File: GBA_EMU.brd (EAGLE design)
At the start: 130.7 x 72.9 mm, 82 parts, among them J1 USB-MINIB-5PIN, J2 AVR_SPI, SW1 LEFT, SW2 RIGHT, SW3 PWR_SWITCH, U1 MIC7221, U2 MICROCHIP_MCP1642B-ADJ, U4 LM4875, U5 Mic5365-2.8Y, U7 AZV321, X2 HEADPHONE

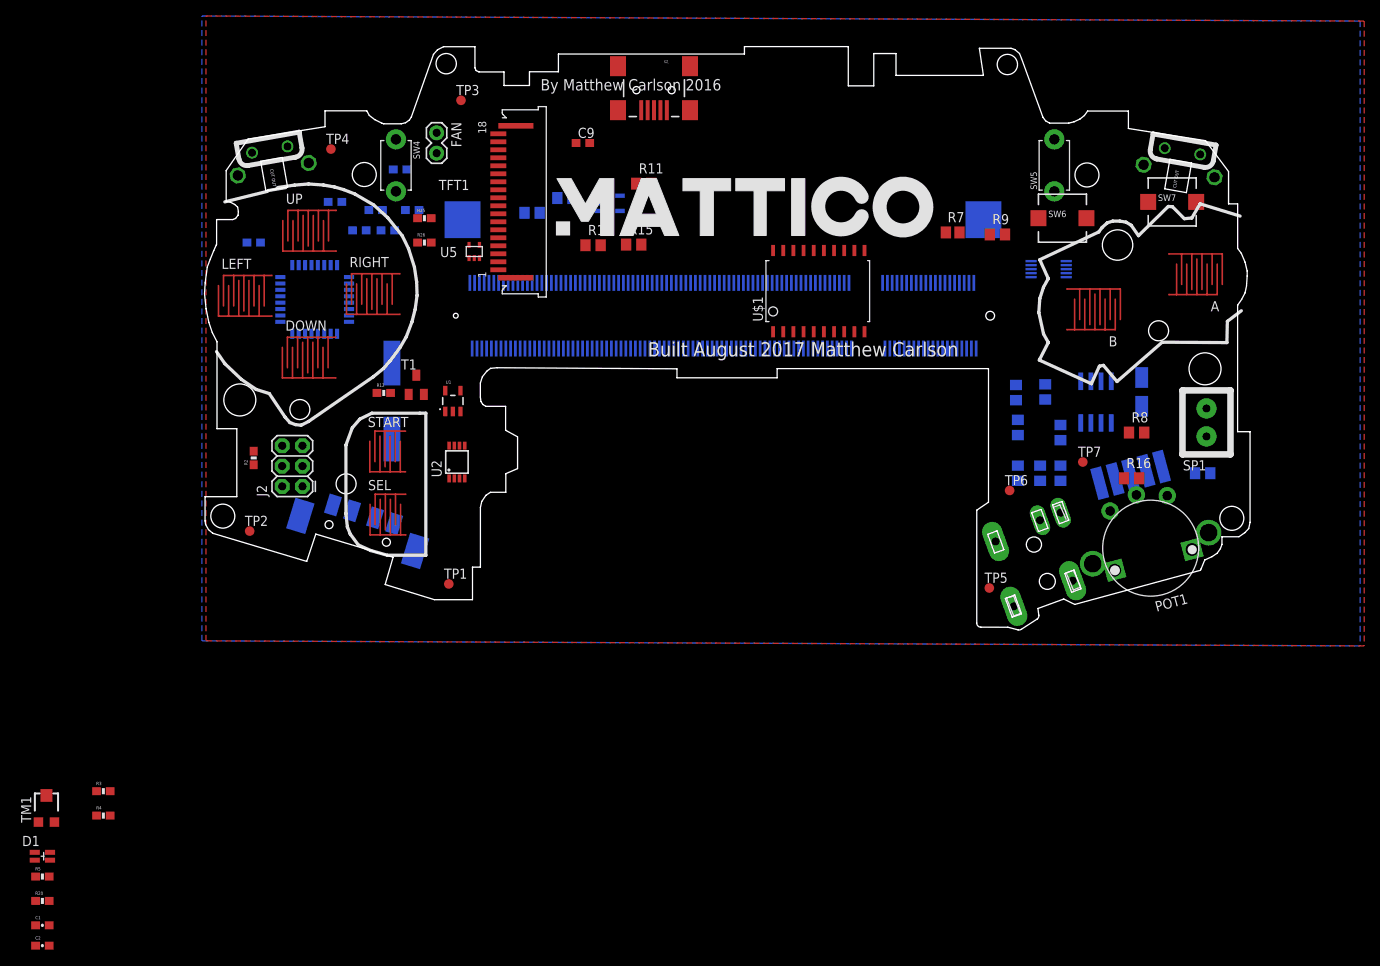
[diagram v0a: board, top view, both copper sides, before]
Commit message: added new parts and routed bus switch
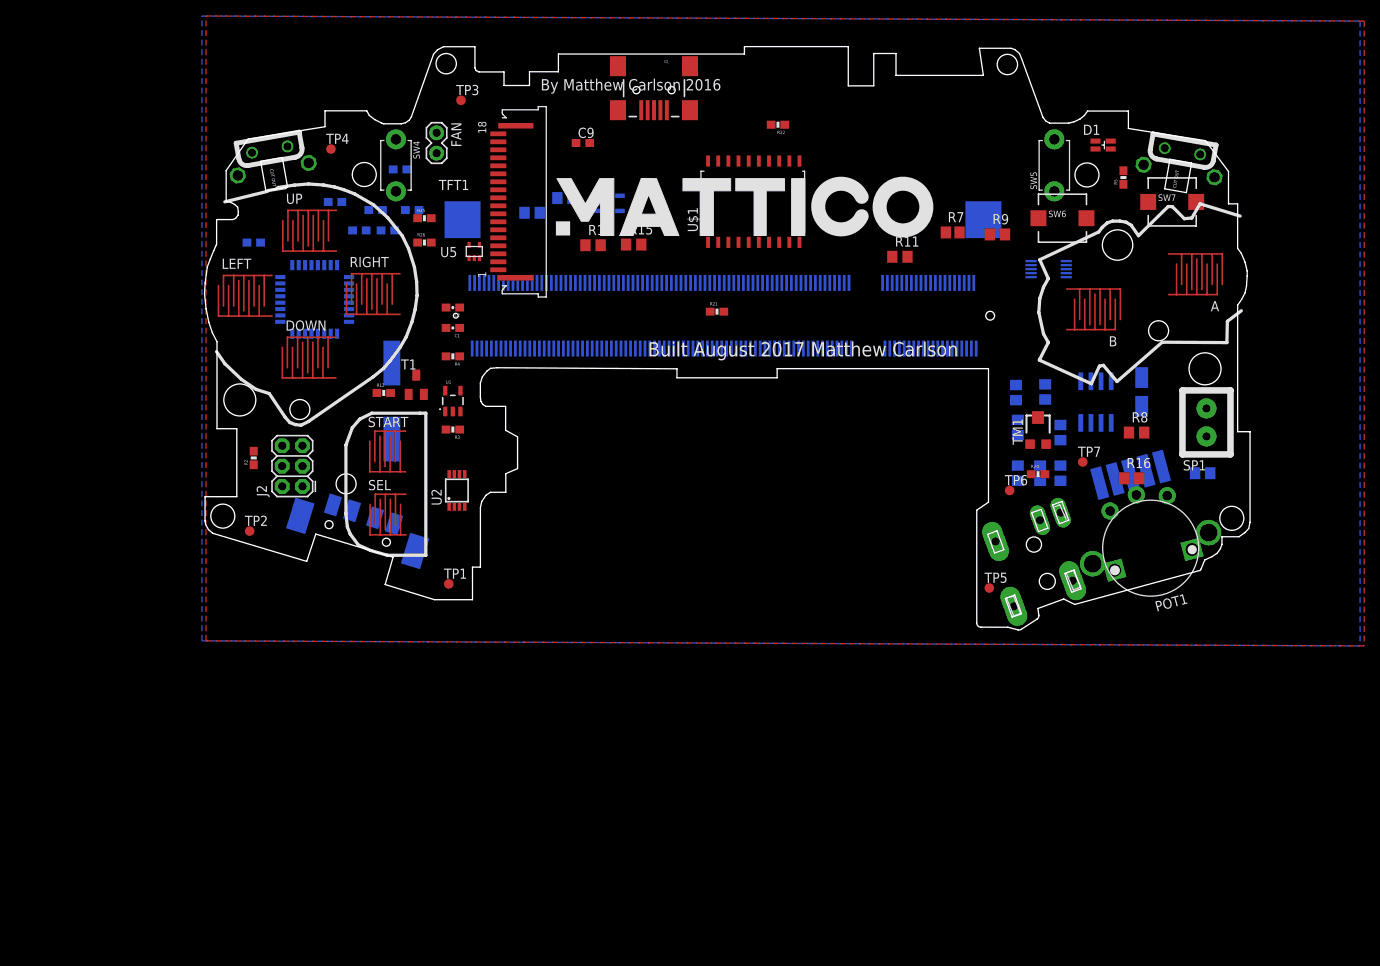
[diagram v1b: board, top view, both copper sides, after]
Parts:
- added R21, R22: 4.7K, SparkFun-Resistors:0603-RES
- moved R5 160.9 mm to (136.1, 65.5), turned to 90 degrees
- moved D1 159.6 mm to (133.6, 69.6)
- moved R20 135.4 mm to (125.5, 28.4)
- moved TM1 132.7 mm to (125.5, 34.0)
- moved C2 94.8 mm to (52.3, 49.3), turned to 180 degrees
- moved C1 90.6 mm to (52.3, 46.7), turned to 180 degrees
- moved R4 72.1 mm to (52.3, 43.2), turned to 180 degrees
- moved R3 62.9 mm to (52.3, 34.0), turned to 180 degrees
- moved R11 33.3 mm to (108.2, 55.6)
- moved U$1 13.8 mm to (84.2, 62.5)
- moved U2 3.56 mm to (52.8, 26.4)
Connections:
- removed net MOSI: TFT1.6
- removed net SCLK: TFT1.3
- removed net VCC: U$1.P$20
- removed net Z_BTN: COPRO.14
- new net COPRO_DC: COPRO.20, U$1.P$8
- new net COPRO_TFT_RESET: COPRO.14, U$1.P$6
- new net N$10: R22.1, U$1.P$19
- new net N$18: R21.1, U$1.P$1
- new net PI_DC: U$1.P$17
- new net PI_MOSI: U$1.P$13
- new net PI_SCK: U$1.P$11
- new net PI_TFT_RESET: U$1.P$15
- new net TFT_MOSI: TFT1.6, U$1.P$16, U$1.P$7
- new net TFT_SCLK: TFT1.3, U$1.P$18, U$1.P$9
- net 3.3V: now also R21.2, R22.2, U$1.P$20
- net COPRO_MOSI: now also U$1.P$4
- net COPRO_SCK: now also U$1.P$2
- net TFT_DC: now also U$1.P$12, U$1.P$3
- net TFT_RESET: now also U$1.P$14, U$1.P$5

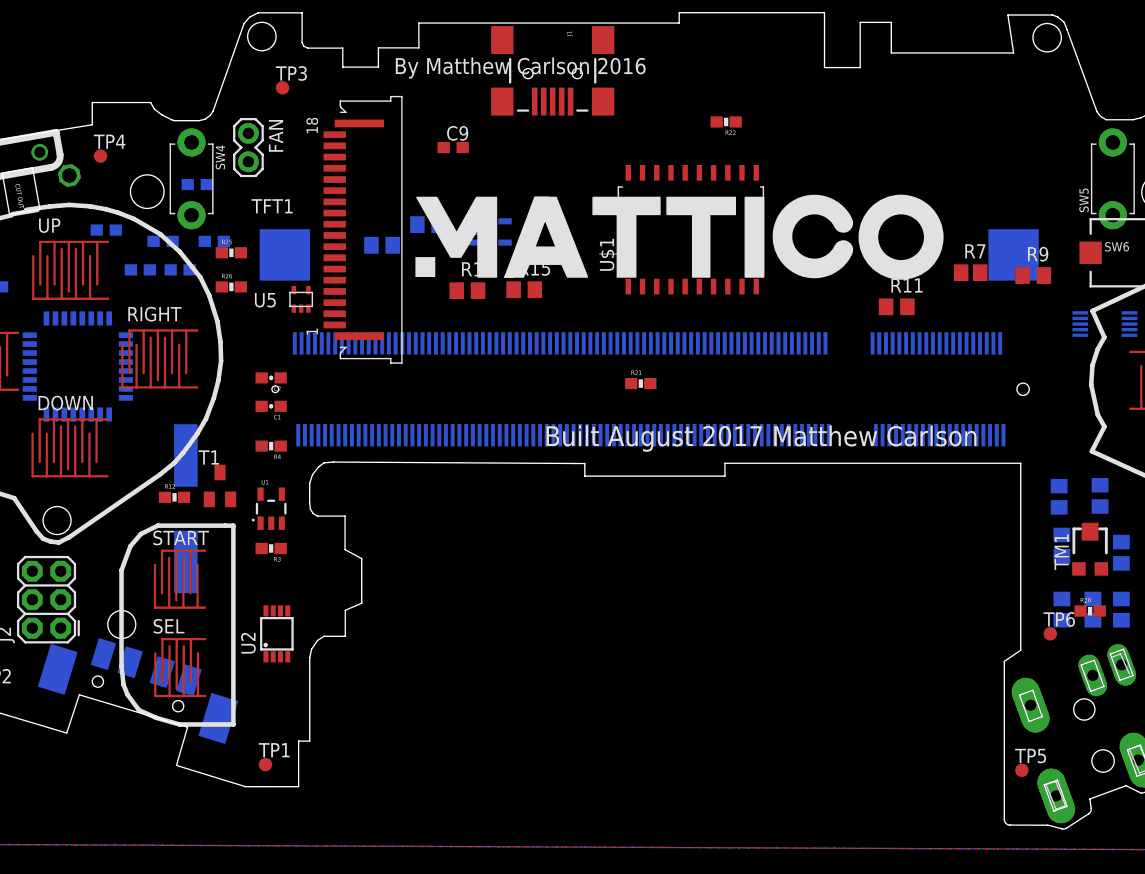
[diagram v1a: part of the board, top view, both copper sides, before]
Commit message: added more to the power circuit
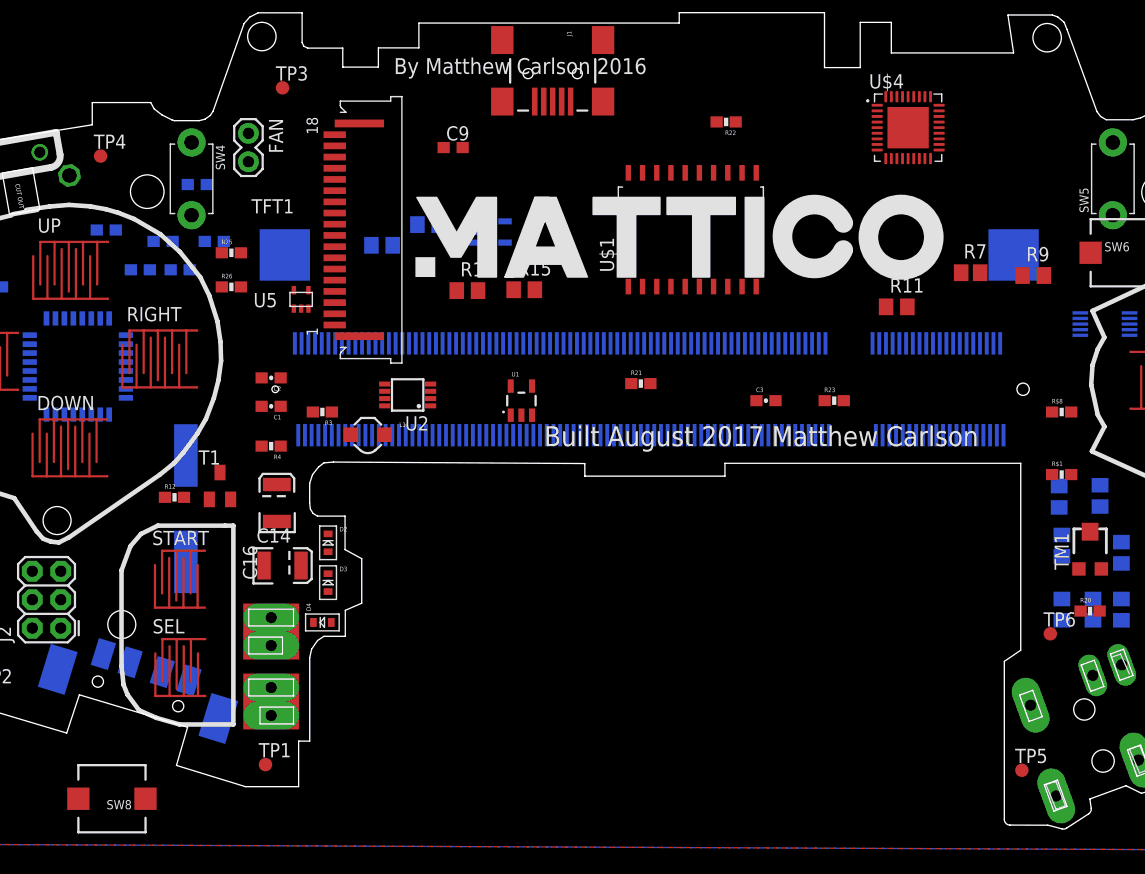
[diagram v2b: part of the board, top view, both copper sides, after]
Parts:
- added BT1: (no value), custom:GBA_BATTERY
- added C14, C16: 47uF, SparkFun-Capacitors:EIA3528
- added C3: 100nF, SparkFun-Capacitors:0603-CAP
- added D2, D3, D4: (no value), adafruit:SOD-523
- added L1: 4.7uH, SparkFun-Passives:INDUCTOR_4.7UH
- added R$1: 976kR, SparkFun-Resistors:0603-RES
- added R$8: 430kR, SparkFun-Resistors:0603-RES
- added R23: 100k, SparkFun-Resistors:0603-RES
- added SW8: (no value), adafruit:PUSHBUTTON_SMD_SJ
- added U$4: USB2523B, custom:QFN37P50_600X600X100L62X24T370N
- U2: value MICROCHIP_MCP1642B-ADJ -> MCP1642B-ADJ
- moved U1 24.3 mm to (74.7, 47.2)
- moved U2 24.3 mm to (64.5, 47.8), turned to 90 degrees
- moved R3 13.0 mm to (56.9, 46.2)
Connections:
- removed net VIN: U2.8
- new net N$23: R$1.1, R$8.2, U2.2
- new net N$30: C16.C
- new net N$31: D2.K, D3.A
- new net N$32: C14.A, L1.P$1, U2.8
- new net N$33: D3.K, D4.A
- new net N$34: L1.P$2, U2.5
- new net VDD33: U$4.15, U$4.23, U$4.29
- new net VDDA33: U$4.10, U$4.36, U$4.5
- net 5V: now also C16.A, C3.1, R$1.2, U2.4
- net GND: now also BT1.BT-1, BT1.BT-2, C14.C, C3.2, R$8.1, U$4.37
- net V_BATT: now also BT1.BT+1, BT1.BT+2, SW8.P$1

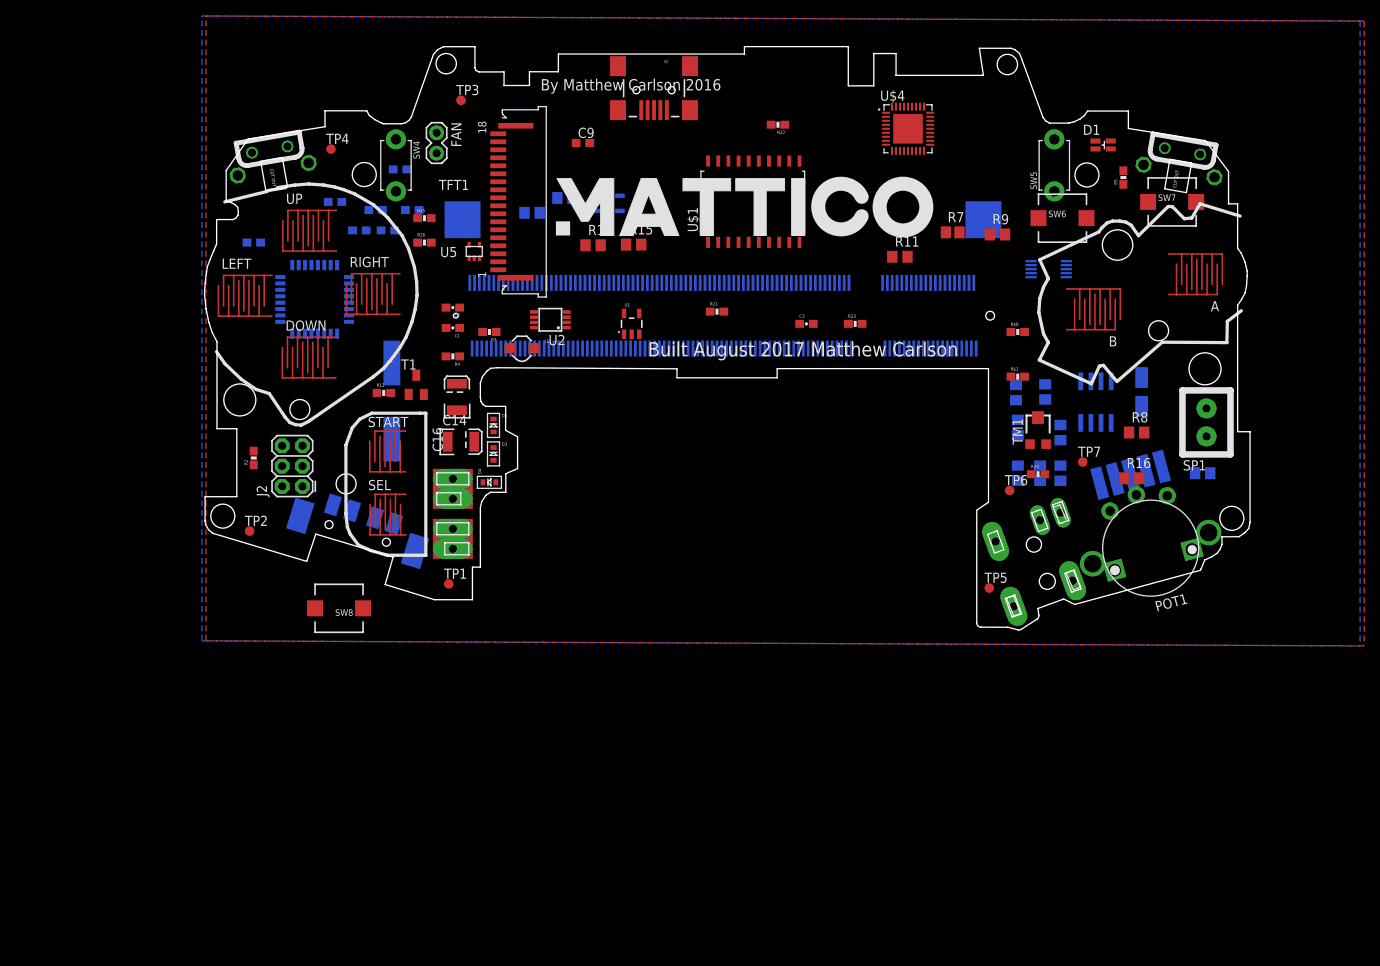
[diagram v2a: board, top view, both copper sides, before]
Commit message: moved all buttons to pi instead of copro
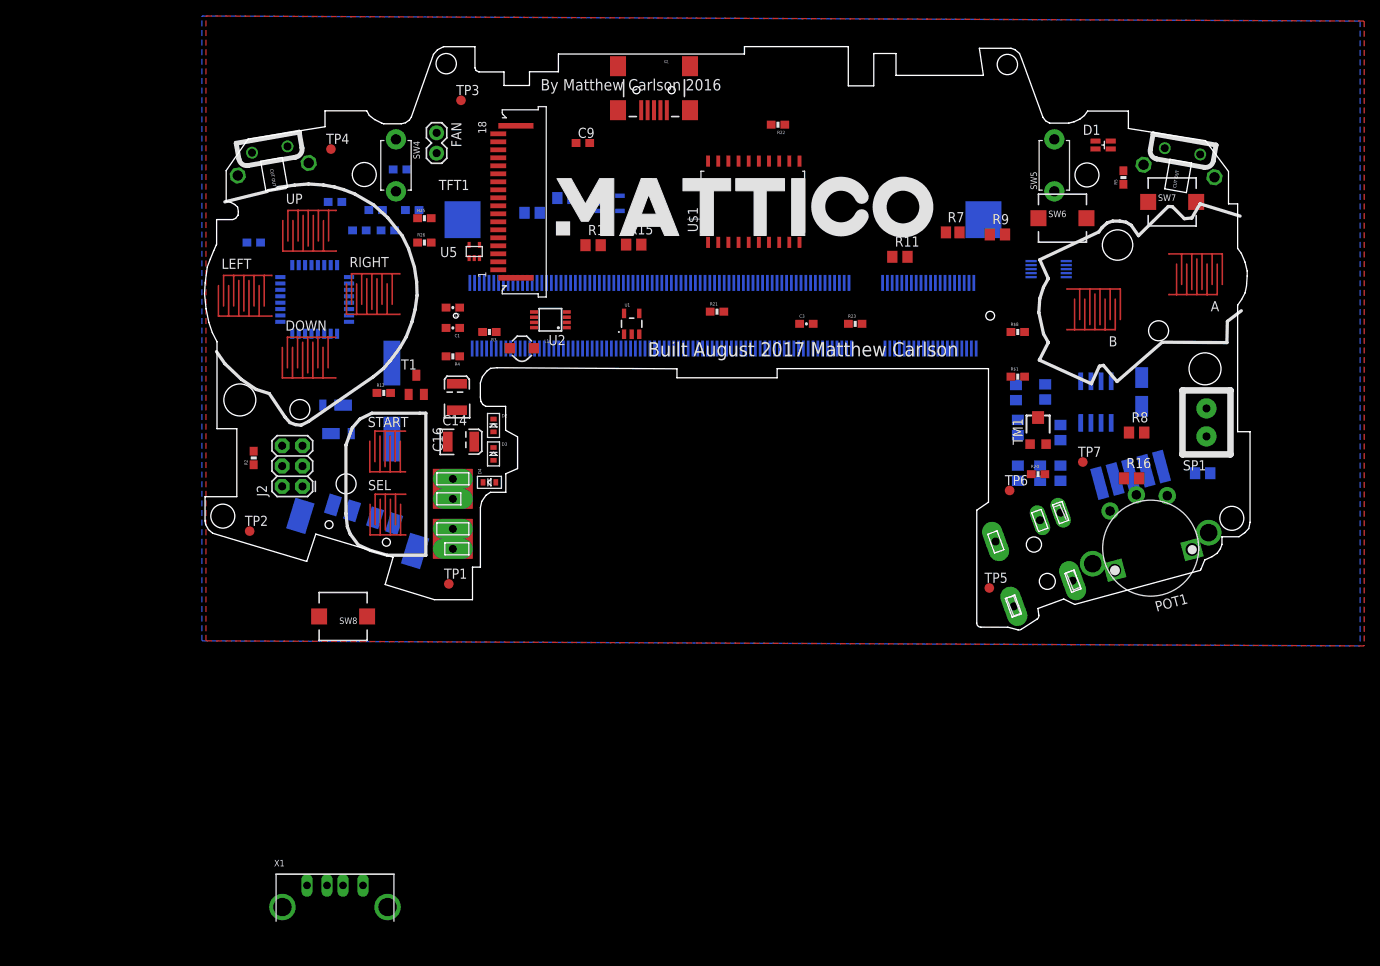
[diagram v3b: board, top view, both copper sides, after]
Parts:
- removed U$4: USB2523B, custom:QFN37P50_600X600X100L62X24T370N
- added D5, D6: (no value), custom:DIODE_POWERDI_123
- added X1: (no value), Adafruit_PowerBoost:MICROBUILDER_USB_HOST-PTH
- moved SW8 1.14 mm to (38.6, 10.7)
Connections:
- removed net DOWN: COPRO.7, DOWN.2
- removed net LEFT: COPRO.23, LEFT.2
- removed net LEFT_BUMP: SW1.2
- removed net PI_DC: U$1.P$17
- removed net PWM0: R8.1
- removed net RIGHT: COPRO.22, RIGHT.2
- removed net RIGHT_BUMP: SW2.2
- removed net SELECT: COPRO.13, SEL.2
- removed net START: COPRO.12, START.2
- removed net UP: COPRO.6, UP.2
- removed net VDD33: U$4.15, U$4.23, U$4.29
- removed net VDDA33: U$4.10, U$4.36, U$4.5
- new net DOWN_BTN: DOWN.2, PCB1.59
- new net L1_BTN: PCB1.21, SW1.2
- new net LEFT_BTN: LEFT.2, PCB1.89
- new net N$35: PCB1.177
- new net N$36: PCB1.197, PCB1.199
- new net N$37: PCB1.198, PCB1.200
- new net PI_PWM0: PCB1.63, R8.1
- new net PI_TFT_DC: PCB1.11, U$1.P$17
- new net PWR_EN: COPRO.6, U2.1
- new net R1_BTN: PCB1.71, SW2.2
- new net RIGHT_BTN: PCB1.75, RIGHT.2
- new net SELECT_BTN: PCB1.81, SEL.2
- new net START_BTN: PCB1.77, START.2
- new net UP_BTN: PCB1.17, UP.2
- net 1.8V: now also TP5.TP
- net 3.3V: now also PCB1.40
- net 5V: now also X1.VBUS
- net A_BTN: now also PCB1.65; no longer COPRO.10
- net B_BTN: now also PCB1.87; no longer COPRO.11
- net GND: now also C16.C, X1.GND; no longer U$4.37
- net L2_BTN: now also PCB1.57; no longer COPRO.26
- net N$12: now also D5.2, D6.2, SW8.P$1; no longer SW3.1
- net N$30: now also PCB1.179; no longer C16.C
- net N$32: now also SW8.P$2
- net PI_MOSI: now also PCB1.33
- net PI_SCK: now also PCB1.35
- net PI_TFT_RESET: now also PCB1.9
- net R2_BTN: now also PCB1.45; no longer COPRO.25
- net TFT_CS: now also COPRO.10
- net TFT_LED: now also PCB1.15
- net V_BATT: now also D6.1; no longer SW8.P$1
- net V_USB: now also D5.1
- net X_BTN: now also PCB1.83; no longer COPRO.21
- net Y_BTN: no longer COPRO.5
